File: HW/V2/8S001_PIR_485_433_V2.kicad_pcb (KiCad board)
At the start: 2 copper layers, 35 x 24 mm, 15 parts, among them J1 SWIM, J2 PIR, J3 485, J4 SerIn, J5 RF, SW1 Sw, U1 L78L05_SOT89, U2 STM8S001J3M, U3 SP3485EN

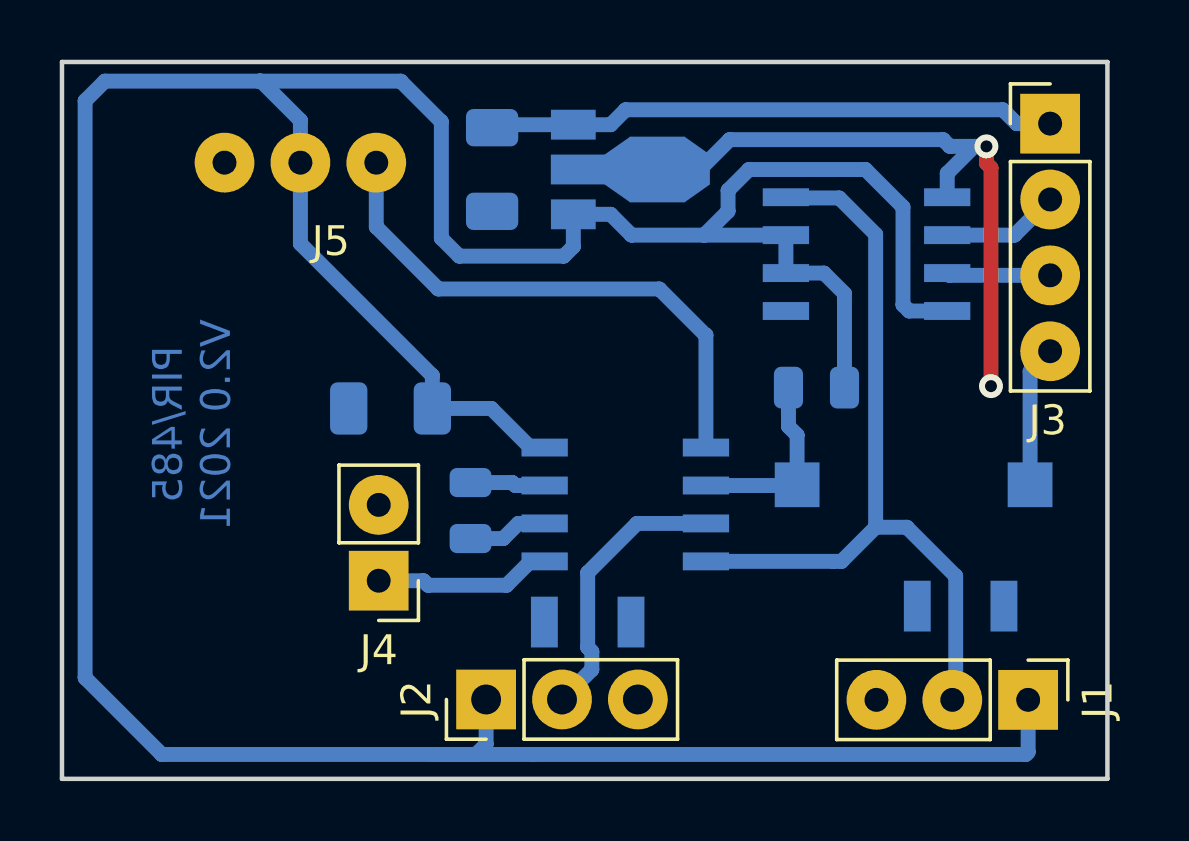
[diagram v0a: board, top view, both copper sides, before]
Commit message: V2.1 HW
MAX485 Data Enable wired to BTN signal, now 485 transmitter can be disabled for multimaster mode
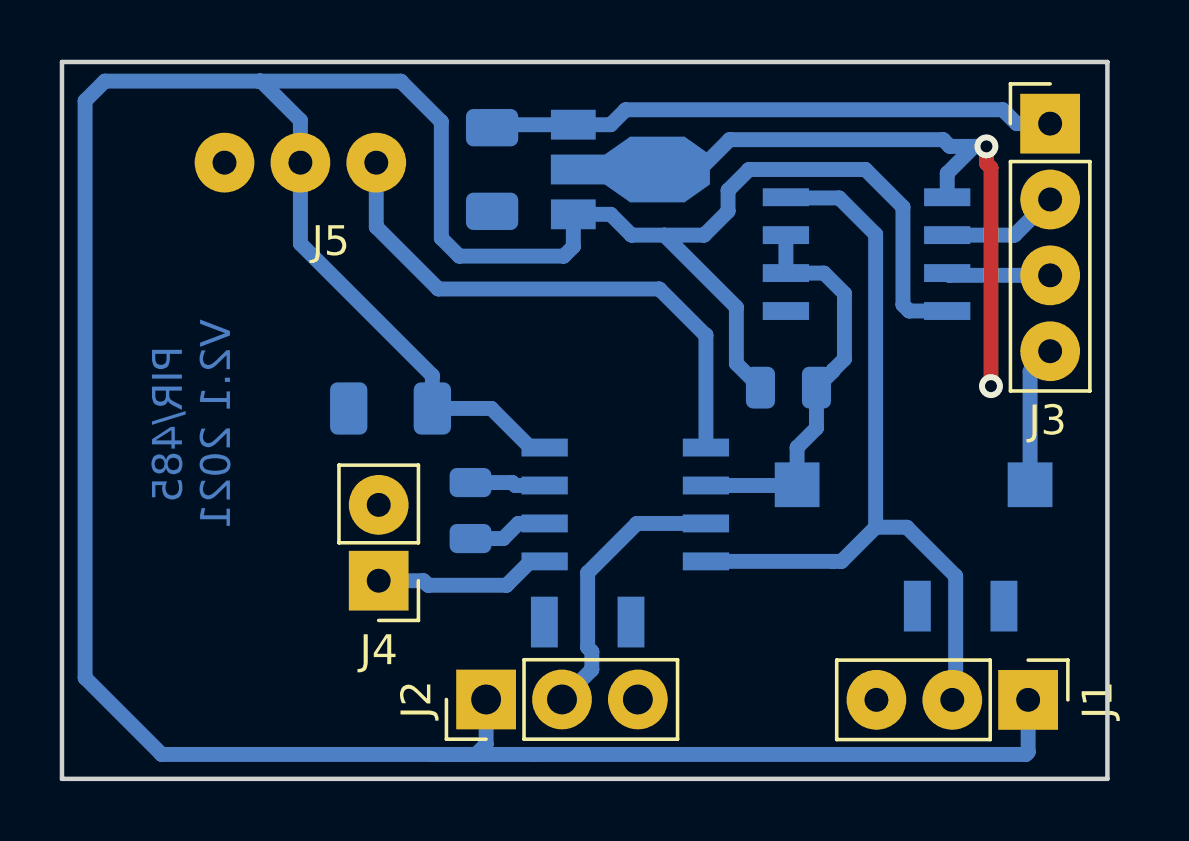
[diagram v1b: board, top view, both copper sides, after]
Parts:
- moved R1 0.94 mm to (54.3, 40.9), turned to 0 degrees
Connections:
- U3 pad 2: +5V -> /BTN
- U3 pad 3: +5V -> /BTN
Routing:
- net /BTN: track 6.43 -> 13.6 mm
- net +5V: track 124.8 -> 121.9 mm
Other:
- board text added: "PIR/485 V2.1 2021"
- board text removed: "PIR/485 V2.0 2021"
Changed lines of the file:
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@@
     (thickness 1.6)
     (drawings 5)
-    (tracks 110)
+    (tracks 116)
     (zones 0)
     (modules 15)
@@
   )
   (module KiCad/kicad-footprints/Resistor_SMD.pretty:R_0805_2012Metric (layer B.Cu)
-    (at 55.26 40.9028 180)
+    (at 54.3225 40.9028)
     (descr "Resistor SMD 0805 (2012 Metric), square (rectangular) end terminal, IPC_7351 nominal, (Body size source: https://docs.google.com/spreadsheets/d/1BsfQQcO9C6DZCsRaXUlFlo91Tg2WpOkGARC1WS5S8t0/edit?usp=sharing), generated with kicad-footprint-generator")
     (tags resistor)
     (attr smd)
-    (fp_text reference R1 (at 0.26 -0.0972 180) (layer B.SilkS)
-      (effects (font (size 1 1) (thickness 0.15)) (justify mirror))
-    )
-    (fp_text value 10K (at 0 -1.65 180) (layer B.Fab)
+    (fp_text reference R1 (at 0.26 -0.0972) (layer B.SilkS)
+      (effects (font (size 1 1) (thickness 0.15)) (justify mirror))
+    )
+    (fp_text value 10K (at 0 -1.65) (layer B.Fab)
       (effects (font (size 1 1) (thickness 0.15)) (justify mirror))
     )
@@
     (fp_line (start 1.68 0.95) (end 1.68 -0.95) (layer B.CrtYd) (width 0.05))
     (fp_line (start 1.68 -0.95) (end -1.68 -0.95) (layer B.CrtYd) (width 0.05))
-    (fp_text user %R (at 0 0 180) (layer B.Fab)
+    (fp_text user %R (at 0 0) (layer B.Fab)
       (effects (font (size 0.5 0.5) (thickness 0.08)) (justify mirror))
     )
-    (pad 1 smd roundrect (at -0.9375 0 180) (size 0.975 1.4) (layers B.Cu B.Paste B.Mask) (roundrect_rratio 0.25)
+    (pad 1 smd roundrect (at -0.9375 0) (size 0.975 1.4) (layers B.Cu B.Paste B.Mask) (roundrect_rratio 0.25)
       (net 2 +5V))
-    (pad 2 smd roundrect (at 0.9375 0 180) (size 0.975 1.4) (layers B.Cu B.Paste B.Mask) (roundrect_rratio 0.25)
+    (pad 2 smd roundrect (at 0.9375 0) (size 0.975 1.4) (layers B.Cu B.Paste B.Mask) (roundrect_rratio 0.25)
       (net 8 /BTN))
     (model ${KISYS3DMOD}/Resistor_SMD.3dshapes/R_0805_2012Metric.wrl
@@
       (net 10 /SWIM_485TX))
     (pad 3 smd rect (at -2.7 -0.635) (size 1.55 0.6) (layers B.Cu B.Paste B.Mask)
-      (net 2 +5V))
+      (net 8 /BTN))
     (pad 2 smd rect (at -2.7 0.635) (size 1.55 0.6) (layers B.Cu B.Paste B.Mask)
-      (net 2 +5V))
+      (net 8 /BTN))
     (pad 1 smd rect (at -2.7 1.905) (size 1.55 0.6) (layers B.Cu B.Paste B.Mask)
       (net 9 "Net-(U3-Pad1)"))
@@
     )
   )
-  (gr_text "PIR/485\nV2.0 2021" (at 34.3558 42.1347 90) (layer B.Cu)
+  (gr_text "PIR/485\nV2.1 2021" (at 34.3558 42.1347 90) (layer B.Cu)
     (effects (font (size 1 1) (thickness 0.2)) (justify mirror))
   )
@@
   (segment (start 45.7896 53.1837) (end 62.2704 53.1837) (width 0.5) (layer B.Cu) (net 2))
   (segment (start 62.2704 53.1837) (end 62.3466 53.1075) (width 0.5) (layer B.Cu) (net 2))
-  (segment (start 46.116 51.1771) (end 46.2811 51.3422) (width 0.5) (layer B.Cu) (net 11) (status 30))
   (segment (start 30.7744 50.6183) (end 33.3398 53.1837) (width 0.5) (layer B.Cu) (net 2))
   (segment (start 30.7744 31.3016) (end 30.7744 50.6183) (width 0.5) (layer B.Cu) (net 2))
@@
   (segment (start 37.982 33.37) (end 37.982 31.955787) (width 0.5) (layer B.Cu) (net 2))
   (segment (start 36.6 30.6412) (end 31.4348 30.6412) (width 0.5) (layer B.Cu) (net 2))
-  (segment (start 55.5114 37.0674) (end 54.2364 37.0674) (width 0.5) (layer B.Cu) (net 2))
-  (segment (start 56.1975 37.7535) (end 55.5114 37.0674) (width 0.5) (layer B.Cu) (net 2))
-  (segment (start 56.1975 40.9028) (end 56.1975 37.7535) (width 0.5) (layer B.Cu) (net 2))
-  (segment (start 54.2364 35.7974) (end 54.2364 37.0674) (width 0.5) (layer B.Cu) (net 2))
+  (segment (start 55.5114 37.0674) (end 54.2364 37.0674) (width 0.5) (layer B.Cu) (net 8))
+  (segment (start 56.1975 37.7535) (end 55.5114 37.0674) (width 0.5) (layer B.Cu) (net 8))
+  (segment (start 54.2364 35.7974) (end 54.2364 37.0674) (width 0.5) (layer B.Cu) (net 8))
   (segment (start 47.12 36.18) (end 47.12 35.1) (width 0.5) (layer B.Cu) (net 2))
   (segment (start 41.3412 30.6412) (end 42.7 32) (width 0.5) (layer B.Cu) (net 2))
@@
   (segment (start 53 33.6) (end 52.3 34.3) (width 0.5) (layer B.Cu) (net 2))
   (segment (start 56.9 33.6) (end 53 33.6) (width 0.5) (layer B.Cu) (net 2))
-  (segment (start 51.5 35.7974) (end 49.0674 35.7974) (width 0.5) (layer B.Cu) (net 2))
-  (segment (start 54.2364 35.7974) (end 51.5 35.7974) (width 0.5) (layer B.Cu) (net 2))
   (segment (start 52.3 34.3) (end 52.3 34.9974) (width 0.5) (layer B.Cu) (net 2))
   (segment (start 59.6364 38.3374) (end 58.3614 38.3374) (width 0.5) (layer B.Cu) (net 2))
@@
   (segment (start 33.3398 53.1837) (end 42.4 53.1837) (width 0.5) (layer B.Cu) (net 2))
   (segment (start 42.4 53.1837) (end 45.7896 53.1837) (width 0.5) (layer B.Cu) (net 2))
+  (segment (start 53.385 40.9028) (end 52.578 40.0958) (width 0.5) (layer B.Cu) (net 2))
+  (segment (start 52.578 38.2104) (end 50.165 35.7974) (width 0.5) (layer B.Cu) (net 2))
+  (segment (start 52.578 40.0958) (end 52.578 38.2104) (width 0.5) (layer B.Cu) (net 2))
+  (segment (start 51.5 35.7974) (end 50.165 35.7974) (width 0.5) (layer B.Cu) (net 2))
+  (segment (start 50.165 35.7974) (end 49.0674 35.7974) (width 0.5) (layer B.Cu) (net 2))
   (segment (start 46.1592 44.1794) (end 45.1762 44.1794) (width 0.5) (layer B.Cu) (net 3) (status 10))
   (segment (start 45.0769 44.0801) (end 43.6776 44.0801) (width 0.5) (layer B.Cu) (net 3) (status 20))
@@
   (segment (start 51.5592 42.9094) (end 51.5592 39.1408) (width 0.5) (layer B.Cu) (net 7))
   (segment (start 51.5592 39.1408) (end 51.55 39.15) (width 0.5) (layer B.Cu) (net 7))
-  (segment (start 54.6112 44.154) (end 54.6112 42.4892) (width 0.5) (layer B.Cu) (net 8) (status 10))
-  (segment (start 54.3225 42.2005) (end 54.3225 40.9028) (width 0.5) (layer B.Cu) (net 8) (status 20))
-  (segment (start 54.6112 42.4892) (end 54.3225 42.2005) (width 0.5) (layer B.Cu) (net 8))
   (segment (start 54.5858 44.1794) (end 54.6112 44.154) (width 0.5) (layer B.Cu) (net 8) (status 30))
   (segment (start 51.5592 44.1794) (end 54.5858 44.1794) (width 0.5) (layer B.Cu) (net 8) (status 30))
+  (segment (start 55.26 42.2552) (end 55.26 40.9028) (width 0.5) (layer B.Cu) (net 8))
+  (segment (start 54.6112 44.154) (end 54.6112 42.904) (width 0.5) (layer B.Cu) (net 8))
+  (segment (start 54.6112 42.904) (end 55.26 42.2552) (width 0.5) (layer B.Cu) (net 8))
+  (segment (start 55.816237 40.346563) (end 55.816237 40.322763) (width 0.5) (layer B.Cu) (net 8))
+  (segment (start 55.26 40.9028) (end 55.816237 40.346563) (width 0.5) (layer B.Cu) (net 8))
+  (segment (start 56.1975 39.9415) (end 56.1975 37.7535) (width 0.5) (layer B.Cu) (net 8))
+  (segment (start 55.816237 40.322763) (end 56.1975 39.9415) (width 0.5) (layer B.Cu) (net 8))
   (segment (start 54.851402 34.5274) (end 54.2364 34.5274) (width 0.5) (layer B.Cu) (net 10) (status 30))
   (segment (start 56.0982 46.7194) (end 57.2412 45.5764) (width 0.5) (layer B.Cu) (net 10))
@@
   (segment (start 59.9209 47.212898) (end 58.284402 45.5764) (width 0.5) (layer B.Cu) (net 10))
   (segment (start 59.9209 51.3422) (end 59.9209 47.212898) (width 0.5) (layer B.Cu) (net 10) (status 10))
+  (segment (start 46.116 51.1771) (end 46.2811 51.3422) (width 0.5) (layer B.Cu) (net 11) (status 30))
   (segment (start 47.739999 50.342201) (end 46.74 51.3422) (width 0.5) (layer B.Cu) (net 11))
   (segment (start 47.739999 49.739999) (end 47.739999 50.342201) (width 0.5) (layer B.Cu) (net 11))
